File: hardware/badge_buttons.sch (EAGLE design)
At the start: 7 parts, among them U2 MLX90614

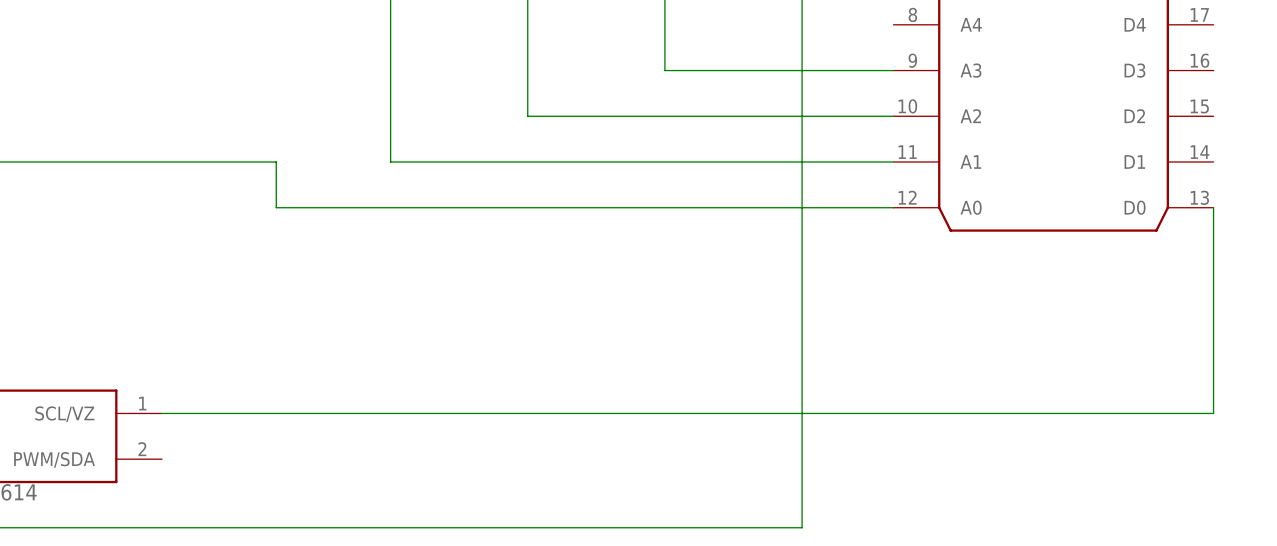
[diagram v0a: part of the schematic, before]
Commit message: refactor directory/finish wiring
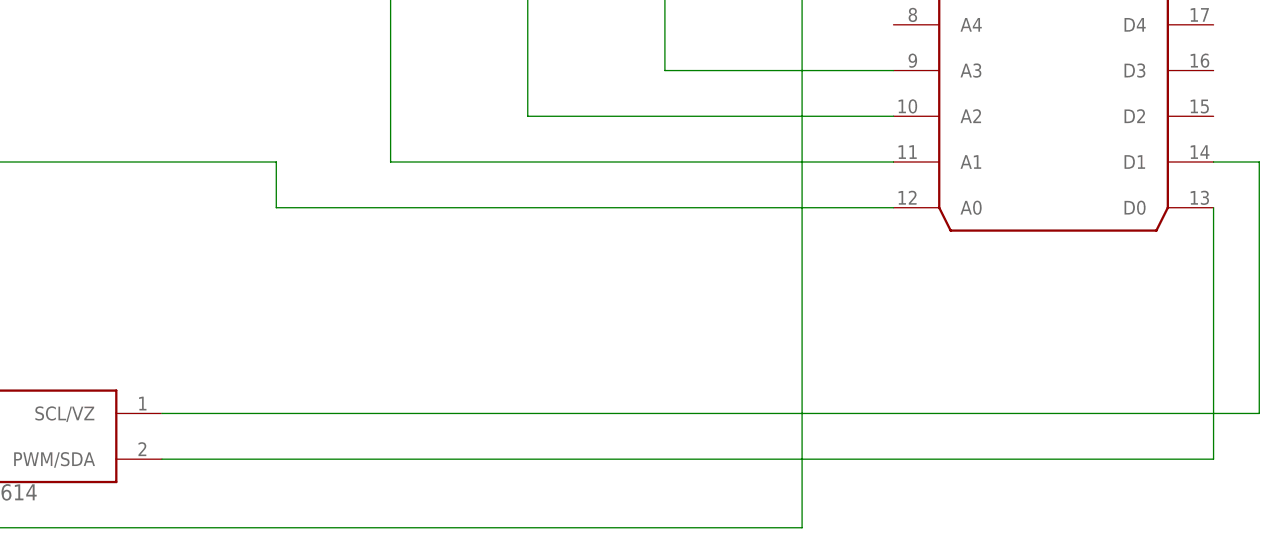
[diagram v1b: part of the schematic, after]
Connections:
- new net N$8: U$1.D1, U2.SCL/VZ
- net N$7: now also U2.PWM/SDA; no longer U2.SCL/VZ
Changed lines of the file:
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@@
 <net name="N$7" class="0">
 <segment>
-<pinref part="U2" gate="G$1" pin="SCL/VZ"/>
+<pinref part="U2" gate="G$1" pin="PWM/SDA"/>
 <pinref part="U$1" gate="G$1" pin="D0"/>
-<wire x1="-2.54" y1="-22.86" x2="114.3" y2="-22.86" width="0.1524" layer="91"/>
-<wire x1="114.3" y1="-22.86" x2="114.3" y2="0" width="0.1524" layer="91"/>
+<wire x1="-2.54" y1="-27.94" x2="114.3" y2="-27.94" width="0.1524" layer="91"/>
+<wire x1="114.3" y1="-27.94" x2="114.3" y2="0" width="0.1524" layer="91"/>
 </segment>
 </net>
+<net name="N$8" class="0">
+<segment>
+<pinref part="U2" gate="G$1" pin="SCL/VZ"/>
+<wire x1="-2.54" y1="-22.86" x2="119.38" y2="-22.86" width="0.1524" layer="91"/>
+<wire x1="119.38" y1="-22.86" x2="119.38" y2="5.08" width="0.1524" layer="91"/>
+<pinref part="U$1" gate="G$1" pin="D1"/>
+<wire x1="119.38" y1="5.08" x2="114.3" y2="5.08" width="0.1524" layer="91"/>
+</segment>
+</net>

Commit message: pusher T
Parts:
- removed U2: MLX90614, SparkFun-Sensors:MLX90614
- added JP1: (no value), jumper:JP4E
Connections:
- new net N$10: JP1.1, U$1.D3
- new net N$9: JP1.2, U$1.D2
- net N$4: no longer U2.VSS
- net N$5: no longer U2.VDD
- net N$7: now also JP1.4; no longer U2.PWM/SDA
- net N$8: now also JP1.3; no longer U2.SCL/VZ
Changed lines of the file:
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@@
 <part name="U1" library="RHT03_DHT-22_AM2302" deviceset="RHT03_DHT-22_AM2302" device=""/>
 <part name="R1" library="resistor" library_urn="urn:adsk.eagle:library:348" deviceset="R-US_" device="0204/7" package3d_urn="urn:adsk.eagle:package:25945/1"/>
-<part name="U2" library="SparkFun-Sensors" deviceset="MLX90614" device=""/>
+<part name="JP1" library="jumper" library_urn="urn:adsk.eagle:library:252" deviceset="JP4E" device="" package3d_urn="urn:adsk.eagle:package:15463/1"/>
 </parts>
 <sheets>
@@
 <instance part="U1" gate="G$1" x="-10.16" y="50.8"/>
 <instance part="R1" gate="G$1" x="-38.1" y="53.34" rot="R90"/>
-<instance part="U2" gate="G$1" x="-17.78" y="-25.4"/>
+<instance part="JP1" gate="G$1" x="-48.26" y="-12.7"/>
 </instances>
 <busses>
@@
 <wire x1="78.74" y1="30.48" x2="68.58" y2="30.48" width="0.1524" layer="91"/>
 <wire x1="68.58" y1="30.48" x2="68.58" y2="50.8" width="0.1524" layer="91"/>
-<pinref part="U2" gate="G$1" pin="VSS"/>
-<wire x1="-33.02" y1="-27.94" x2="-38.1" y2="-27.94" width="0.1524" layer="91"/>
-<wire x1="-38.1" y1="-27.94" x2="-38.1" y2="-35.56" width="0.1524" layer="91"/>
-<wire x1="-38.1" y1="-35.56" x2="68.58" y2="-35.56" width="0.1524" layer="91"/>
-<wire x1="68.58" y1="-35.56" x2="68.58" y2="30.48" width="0.1524" layer="91"/>
 </segment>
 </net>
@@
 <pinref part="R1" gate="G$1" pin="2"/>
 <junction x="-38.1" y="58.42"/>
-<wire x1="-38.1" y1="58.42" x2="-43.18" y2="58.42" width="0.1524" layer="91"/>
-<pinref part="U2" gate="G$1" pin="VDD"/>
-<wire x1="-43.18" y1="58.42" x2="-43.18" y2="-22.86" width="0.1524" layer="91"/>
-<wire x1="-43.18" y1="-22.86" x2="-33.02" y2="-22.86" width="0.1524" layer="91"/>
 </segment>
 </net>
@@
 <net name="N$7" class="0">
 <segment>
-<pinref part="U2" gate="G$1" pin="PWM/SDA"/>
+<pinref part="JP1" gate="G$1" pin="4"/>
+<wire x1="-43.18" y1="-15.24" x2="-43.18" y2="-20.32" width="0.1524" layer="91"/>
 <pinref part="U$1" gate="G$1" pin="D0"/>
-<wire x1="-2.54" y1="-27.94" x2="114.3" y2="-27.94" width="0.1524" layer="91"/>
-<wire x1="114.3" y1="-27.94" x2="114.3" y2="0" width="0.1524" layer="91"/>
+<wire x1="-43.18" y1="-20.32" x2="114.3" y2="-20.32" width="0.1524" layer="91"/>
+<wire x1="114.3" y1="-20.32" x2="114.3" y2="0" width="0.1524" layer="91"/>
 </segment>
 </net>
 <net name="N$8" class="0">
 <segment>
-<pinref part="U2" gate="G$1" pin="SCL/VZ"/>
-<wire x1="-2.54" y1="-22.86" x2="119.38" y2="-22.86" width="0.1524" layer="91"/>
-<wire x1="119.38" y1="-22.86" x2="119.38" y2="5.08" width="0.1524" layer="91"/>
+<pinref part="JP1" gate="G$1" pin="3"/>
+<wire x1="-45.72" y1="-15.24" x2="-45.72" y2="-25.4" width="0.1524" layer="91"/>
+<wire x1="-45.72" y1="-25.4" x2="116.84" y2="-25.4" width="0.1524" layer="91"/>
+<wire x1="116.84" y1="-25.4" x2="116.84" y2="5.08" width="0.1524" layer="91"/>
 <pinref part="U$1" gate="G$1" pin="D1"/>
-<wire x1="119.38" y1="5.08" x2="114.3" y2="5.08" width="0.1524" layer="91"/>
+<wire x1="116.84" y1="5.08" x2="114.3" y2="5.08" width="0.1524" layer="91"/>
 </segment>
 </net>
+<net name="N$9" class="0">
+<segment>
+<pinref part="JP1" gate="G$1" pin="2"/>
+<wire x1="-48.26" y1="-15.24" x2="-48.26" y2="-27.94" width="0.1524" layer="91"/>
+<wire x1="-48.26" y1="-27.94" x2="119.38" y2="-27.94" width="0.1524" layer="91"/>
+<wire x1="119.38" y1="-27.94" x2="119.38" y2="10.16" width="0.1524" layer="91"/>
+<pinref part="U$1" gate="G$1" pin="D2"/>
+<wire x1="119.38" y1="10.16" x2="114.3" y2="10.16" width="0.1524" layer="91"/>
+</segment>
+</net>
+<net name="N$10" class="0">
+<segment>
+<pinref part="JP1" gate="G$1" pin="1"/>
+<wire x1="-50.8" y1="-15.24" x2="-50.8" y2="-30.48" width="0.1524" layer="91"/>
+<wire x1="-50.8" y1="-30.48" x2="121.92" y2="-30.48" width="0.1524" layer="91"/>
+<wire x1="121.92" y1="-30.48" x2="121.92" y2="15.24" width="0.1524" layer="91"/>
+<pinref part="U$1" gate="G$1" pin="D3"/>
+<wire x1="121.92" y1="15.24" x2="114.3" y2="15.24" width="0.1524" layer="91"/>
+</segment>
+</net>
